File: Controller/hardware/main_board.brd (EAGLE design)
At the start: 75 x 59 mm, 45 parts, among them IC1 LINEAR_78DT, IC2 40XX_4050D, IC3 LP298XS, IC5 ATMEGA328, Q4 16MHZ, X1 MICROSD_SMD, X4 CON-PHOENIX-508_MST2V

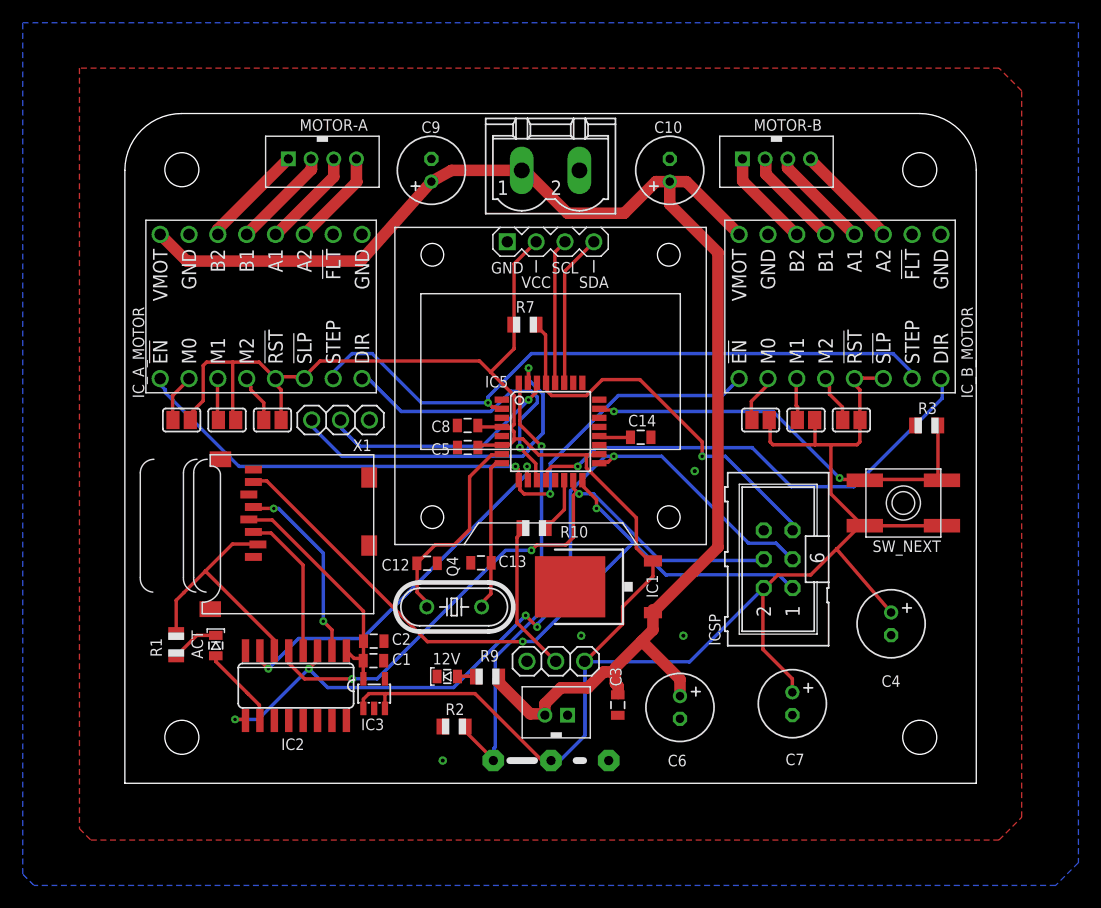
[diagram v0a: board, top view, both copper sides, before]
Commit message: final cleanup
little more silk screen shuffling and clearing DRC errors
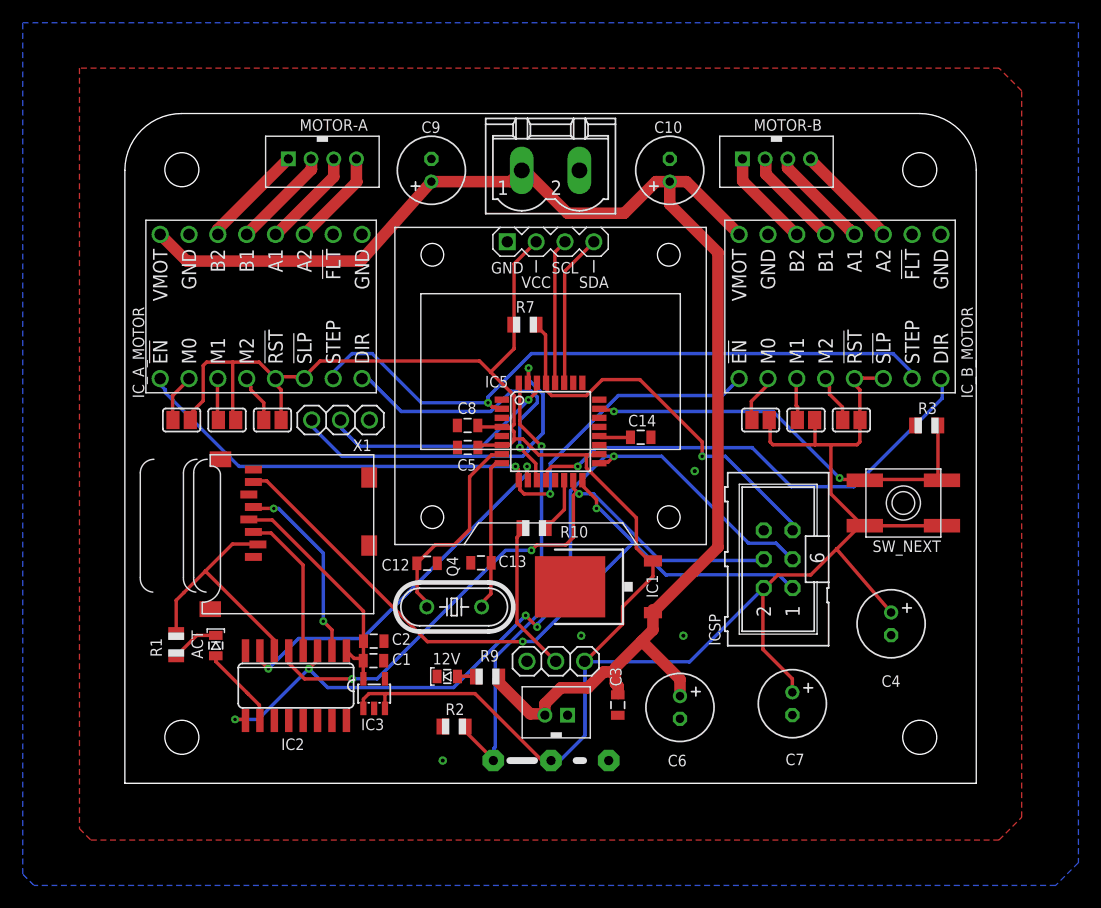
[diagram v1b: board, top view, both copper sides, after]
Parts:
- 12V: value (none) -> 12v
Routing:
- net N$19: track 9.01 -> 9.75 mm

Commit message: updated board name
changed board name to reflect copper changes
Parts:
- 12V: value 12v -> (none); device main_board:SPARKFUN_LED-0805 -> SparkFun:LED-0805
- ACT: value ACT -> RED; device main_board:SPARKFUN_LED-0805 -> adafruit:CHIP-LED0805
- C1: value 10uF -> 10uF/10V; device main_board:SPARKFUN_0805 -> adafruit:A/3216-18R
- C10, C4, C6, C7, C9: device main_board:RCL_E3,5-8 -> rcl:E3,5-8
- C12, C13: value 16pF -> 16pf; device main_board:SPARKFUN_0805 -> SparkFun:0805
- C14, C3, C5, C8: value 0.1uF -> 100nF; device main_board:SPARKFUN_0805 -> SparkFun:0805
- C2: device main_board:SPARKFUN_0805 -> adafruit:C0805K
- IC1: value LINEAR_78DT -> 7805DT; device main_board:LINEAR_TO252 -> linear:TO252
- IC2: value 40XX_4050D -> 4050D; device main_board:40XX_SO16 -> 40xx:SO16
- IC3: device main_board:ADAFRUIT_SOT23-5L -> adafruit:SOT23-5L
- IC5: device main_board:SPARKFUN_TQFP32-08 -> SparkFun:TQFP32-08
- ICSP: device main_board:CON-HARTING-ML_ML6 -> con-harting-ml:ML6
- IC_A_MOTOR, IC_B_MOTOR: value POLOLU-STEPPER-DRIVER_2133-DRV8825 -> 2133-DRV8825; device main_board:POLOLU-STEPPER-DRIVER_DRV8825 -> pololu-stepper-driver:DRV8825
- J1: device main_board:JUMPER_05C -> jumper:05C
- JP1, JP5: device main_board:ADAFRUIT_1X03 -> adafruit:1X03
- JP4: value JST_EPH_2PIN -> 2PIN; device main_board:JST_EPH_B2B-PH-K-S -> jst_eph:B2B-PH-K-S
- MOTOR-A, MOTOR-B: value JST_EPH_4PIN -> 4PIN; device main_board:JST_EPH_B4B-PH-K-S -> jst_eph:B4B-PH-K-S
- Q4: device main_board:CRYSTAL_HC49/S -> crystal:HC49/S
- R1: value 1.0k -> 1K; device main_board:ADAFRUIT_R0805 -> adafruit:R0805
- R10: value 330 -> 330r; device main_board:ADAFRUIT_R0805 -> adafruit:R0805
- R2, R3: value 10k -> 10K; device main_board:ADAFRUIT_R0805 -> adafruit:R0805
- R7: value 10k -> 10K; device main_board:ADAFRUIT_R0805 -> SparkFun:0805
- R9: value 2.2k -> 2.2K; device main_board:ADAFRUIT_R0805 -> SparkFun:0805
- SJ1, SJ2, SJ3, SJ4, SJ5, SJ6: device main_board:JUMPER_SJ -> jumper:SJ
- SW_NEXT: device main_board:ADAFRUIT_EVQ-Q2 -> adafruit:EVQ-Q2
- U$1: value DIY-MODULES_DISPLAY-OLED-128X64-I2C -> DISPLAY-OLED-128X64-I2C; device main_board:DIY-MODULES_DISPLAY-OLED-128X64-I2C -> diy-modules:DISPLAY-OLED-128X64-I2C
- X1: value MICROSD_SMD -> MICROSD; device main_board:ADAFRUIT_MICROSD -> adafruit:MICROSD
- X4: value CON-PHOENIX-508_MST2V -> MST2V; device main_board:CON-PHOENIX-508_MSTBV2 -> con-phoenix-508:MSTBV2
- moved C1 10.4 mm to (15.4, 2.63)
- moved C2 10.3 mm to (24.4, 2.52)
- moved C5 3.13 mm to (27.5, 31.2), turned to 270 degrees
- moved IC3 2.24 mm to (24.0, 8.90)
- moved C4 1.90 mm to (67.5, 15.9), turned to 90 degrees
- moved ACT 1.58 mm to (9.39, 11.4), turned to 180 degrees
- moved IC2 1.41 mm to (16.1, 9.60)
- moved C6 1.29 mm to (49.3, 7.90), turned to 0 degrees
- moved C14 1.00 mm to (46.4, 30.5)
- moved C7 0.81 mm to (59.0, 7.80), turned to 0 degrees
- moved R1 0.74 mm to (4.79, 11.5), turned to 0 degrees
- moved C8 0.61 mm to (29.7, 31.2), turned to 90 degrees
- turned C10 to 0 degrees
- turned C9 to 180 degrees
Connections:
- net +3V3: now also C1.+; no longer C1.1, C2.1
- net GND: now also C1.-; no longer C1.2
- net VCC: now also C2.1
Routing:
- net +3V3: track 21.8 -> 35.1 mm
- net GND: track 0.00 -> 12.7 mm
- net N$31: track 18.4 -> 22.8 mm
- net VCC: track 215.9 -> 218.3 mm
- net N$3: track 21.7 -> 23.8 mm
- net D13: track 74.5 -> 73.1 mm
- net N$2: track 16.8 -> 15.4 mm
- net D6: track 33.7 -> 32.3 mm
- net N$20: track 2.80 -> 4.12 mm
- net N$14: track 9.04 -> 10.1 mm
- net N$13: track 9.25 -> 10.3 mm
- net N$16: track 8.58 -> 9.51 mm
- net D2: track 39.9 -> 40.8 mm
- net A0: track 37.7 -> 38.4 mm
- net D11: track 56.4 -> 55.7 mm
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
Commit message: changed part reference to project specific library and updated capacitor parts
updated capacitor parts with part numbers
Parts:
- 12V: device SparkFun:LED-0805 -> main_board:SPARKFUN_LED-0805
- ACT: device adafruit:CHIP-LED0805 -> main_board:ADAFRUIT_CHIP-LED0805
- C1: value 10uF/10V -> 10uF; device adafruit:A/3216-18R -> main_board:SPARKFUN_0805
- C10, C4, C6, C7, C9: device rcl:E3,5-8 -> main_board:RCL_E3,5-8
- C12, C13: value 16pf -> 16pF; device SparkFun:0805 -> main_board:SPARKFUN_0805
- C14, C3, C5, C8: value 100nF -> 0.1uF; device SparkFun:0805 -> main_board:SPARKFUN_0805
- C2: device adafruit:C0805K -> main_board:SPARKFUN_0805
- IC1: value 7805DT -> LINEAR_7805DT; device linear:TO252 -> main_board:LINEAR_TO252
- IC2: value 4050D -> 40XX_4050D; device 40xx:SO16 -> main_board:40XX_SO16
- IC3: value LP298XS -> ADAFRUIT_LP298XS; device adafruit:SOT23-5L -> main_board:ADAFRUIT_SOT23-5L
- IC5: device SparkFun:TQFP32-08 -> main_board:SPARKFUN_TQFP32-08
- ICSP: device con-harting-ml:ML6 -> main_board:CON-HARTING-ML_ML6
- IC_A_MOTOR, IC_B_MOTOR: value 2133-DRV8825 -> POLOLU-STEPPER-DRIVER_2133-DRV8825; device pololu-stepper-driver:DRV8825 -> main_board:POLOLU-STEPPER-DRIVER_DRV8825
- J1: device jumper:05C -> main_board:JUMPER_05C
- JP1, JP5: device adafruit:1X03 -> main_board:ADAFRUIT_1X03
- JP4: value 2PIN -> JST_EPH_2PIN; device jst_eph:B2B-PH-K-S -> main_board:JST_EPH_B2B-PH-K-S
- MOTOR-A, MOTOR-B: value 4PIN -> JST_EPH_4PIN; device jst_eph:B4B-PH-K-S -> main_board:JST_EPH_B4B-PH-K-S
- Q4: device crystal:HC49/S -> main_board:CRYSTAL_HC49/S
- R1, R10, R2, R3: device adafruit:R0805 -> main_board:ADAFRUIT_R0805
- R7, R9: device SparkFun:0805 -> main_board:SPARKFUN_0805
- SJ1, SJ2, SJ3, SJ4, SJ5, SJ6: device jumper:SJ -> main_board:JUMPER_SJ
- SW_NEXT: device adafruit:EVQ-Q2 -> main_board:ADAFRUIT_EVQ-Q2
- U$1: value DISPLAY-OLED-128X64-I2C -> DIY-MODULES_DISPLAY-OLED-128X64-I2C; device diy-modules:DISPLAY-OLED-128X64-I2C -> main_board:DIY-MODULES_DISPLAY-OLED-128X64-I2C
- X1: value MICROSD -> ADAFRUIT_MICROSD; device adafruit:MICROSD -> main_board:ADAFRUIT_MICROSD
- X4: value MST2V -> CON-PHOENIX-508_MST2V; device con-phoenix-508:MSTBV2 -> main_board:CON-PHOENIX-508_MSTBV2
- moved C1 12.1 mm to (22.8, 12.3)
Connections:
- net +3V3: now also C1.1; no longer C1.+
- net GND: now also C1.2; no longer C1.-
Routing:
- net +3V3: track 35.1 -> 21.4 mm

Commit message: added part numbers, consolidated parts,  cleaned up board/schematic
added part numbers for capacitors, resistors, ic's and the main 12v connector.

cleaned up the board layout a little, mainly just straightening traces.

fixed the through hole 100uf cap footprint to reflect the bom part, 2mm leads 5mm body

made both leds the same part number.

removed the polarized caps from the sd card and replaced with smd 0805 ceramic caps.

cleaned up the schematic a little and added a frame
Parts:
- ACT: value RED -> ACT; device main_board:ADAFRUIT_CHIP-LED0805 -> main_board:SPARKFUN_LED-0805
- IC1: value LINEAR_7805DT -> LINEAR_78DT
- IC3: value ADAFRUIT_LP298XS -> LP298XS
- R1: value 1K -> 1.0k
- R10: value 330r -> 330
- R2, R3: value 10K -> 10k
- R7: value 10K -> 10k; device main_board:SPARKFUN_0805 -> main_board:ADAFRUIT_R0805
- R9: value 2.2K -> 2.2k; device main_board:SPARKFUN_0805 -> main_board:ADAFRUIT_R0805
- X1: value ADAFRUIT_MICROSD -> MICROSD_SMD
- moved C2 10.3 mm to (21.9, 12.5)
- moved C5 3.13 mm to (30.2, 29.6), turned to 180 degrees
- moved IC3 2.24 mm to (22.0, 7.90)
- moved C4 1.90 mm to (67.5, 14.1), turned to 270 degrees
- moved C1 1.75 mm to (21.9, 10.8)
- moved ACT 1.58 mm to (8.01, 12.1), turned to 0 degrees
- moved IC2 1.41 mm to (15.1, 8.60)
- moved C6 1.29 mm to (48.9, 6.68), turned to 270 degrees
- moved C14 1.00 mm to (45.4, 30.5)
- moved C7 0.81 mm to (58.8, 7.01), turned to 270 degrees
- moved R1 0.74 mm to (4.52, 12.2), turned to 270 degrees
- moved C8 0.61 mm to (30.2, 31.5), turned to 0 degrees
- turned C10 to 90 degrees
- turned C9 to 90 degrees
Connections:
- net +3V3: now also C2.1
- net VCC: no longer C2.1
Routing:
- net GND: track 12.7 -> 0.00 mm
- net N$31: track 22.8 -> 18.4 mm
- net VCC: track 218.4 -> 215.5 mm
- net N$3: track 23.8 -> 21.7 mm
- net N$2: track 15.4 -> 16.8 mm
- net D6: track 32.3 -> 33.7 mm
- net +12V: track 132.2 -> 130.8 mm
- net N$20: track 4.12 -> 2.80 mm
- net D13: track 73.1 -> 74.4 mm
- net N$14: track 10.1 -> 8.94 mm
- net N$13: track 10.3 -> 9.25 mm
- net N$16: track 9.51 -> 8.58 mm
- net A0: track 38.4 -> 37.6 mm
- net D2: track 40.8 -> 39.9 mm
- net N$19: track 9.76 -> 9.01 mm
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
